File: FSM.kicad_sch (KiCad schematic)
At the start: 6 parts, among them U18 74HCT04, U23 74HCT02, U25 74HCT00, U27 74HCT02, U28 74HCT02, U9 74HCT74

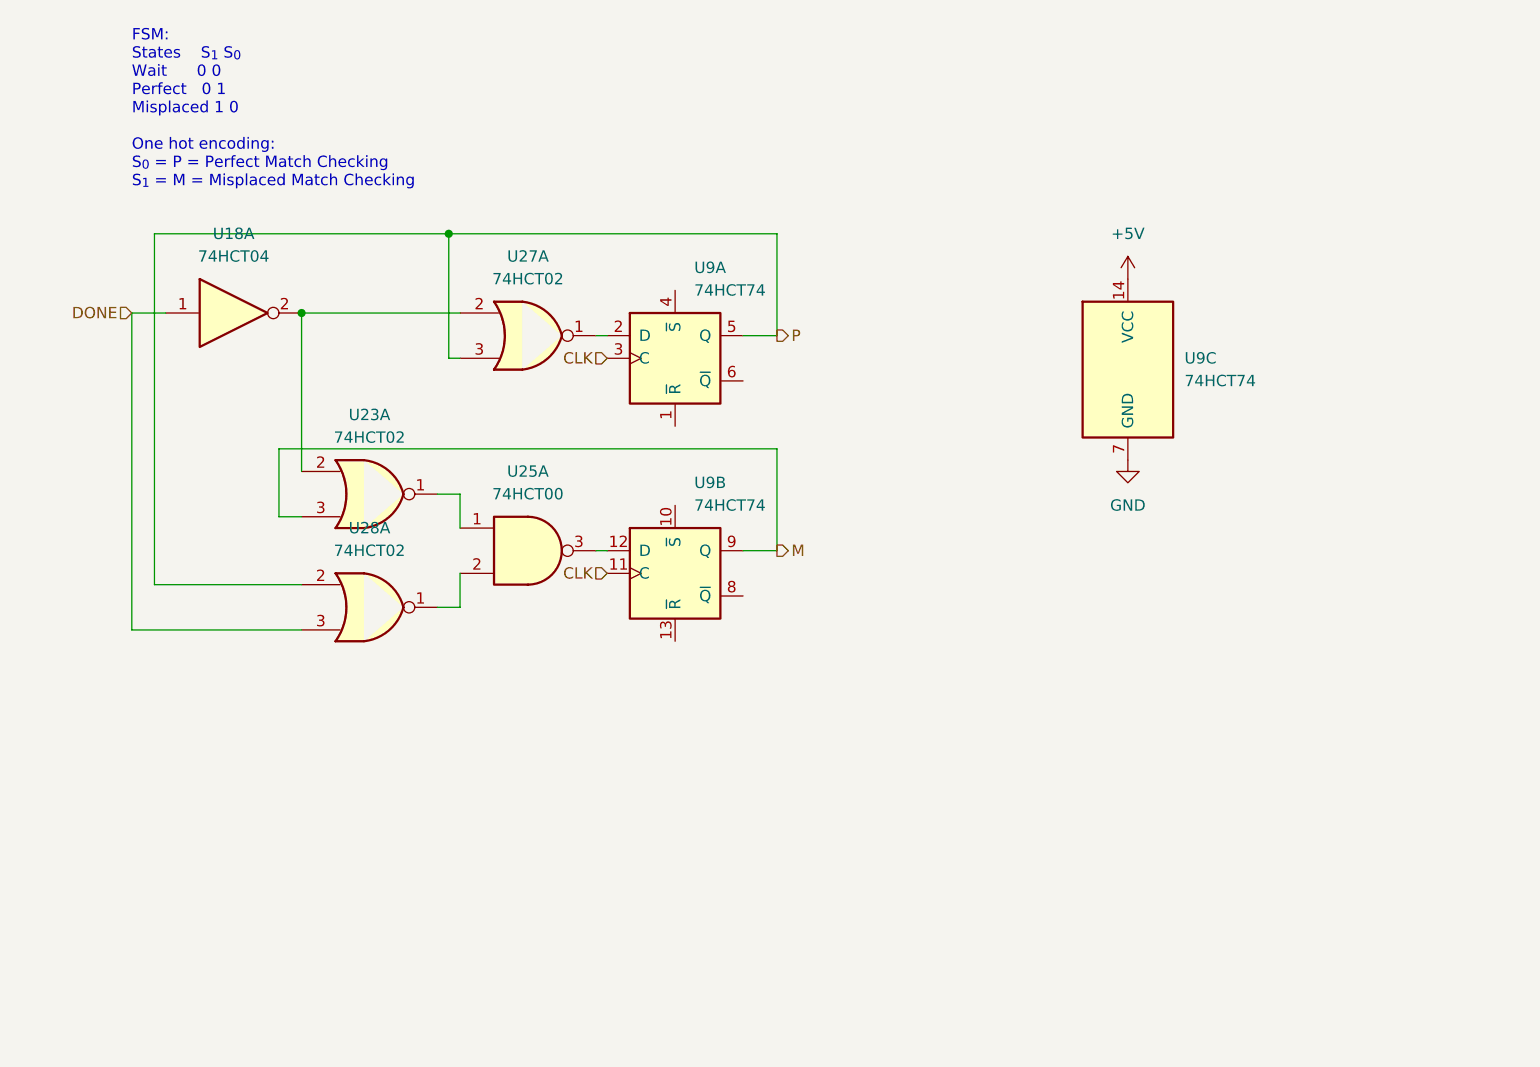
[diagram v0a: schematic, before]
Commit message: Added FSM, Button, 555 timer, changed shift registers
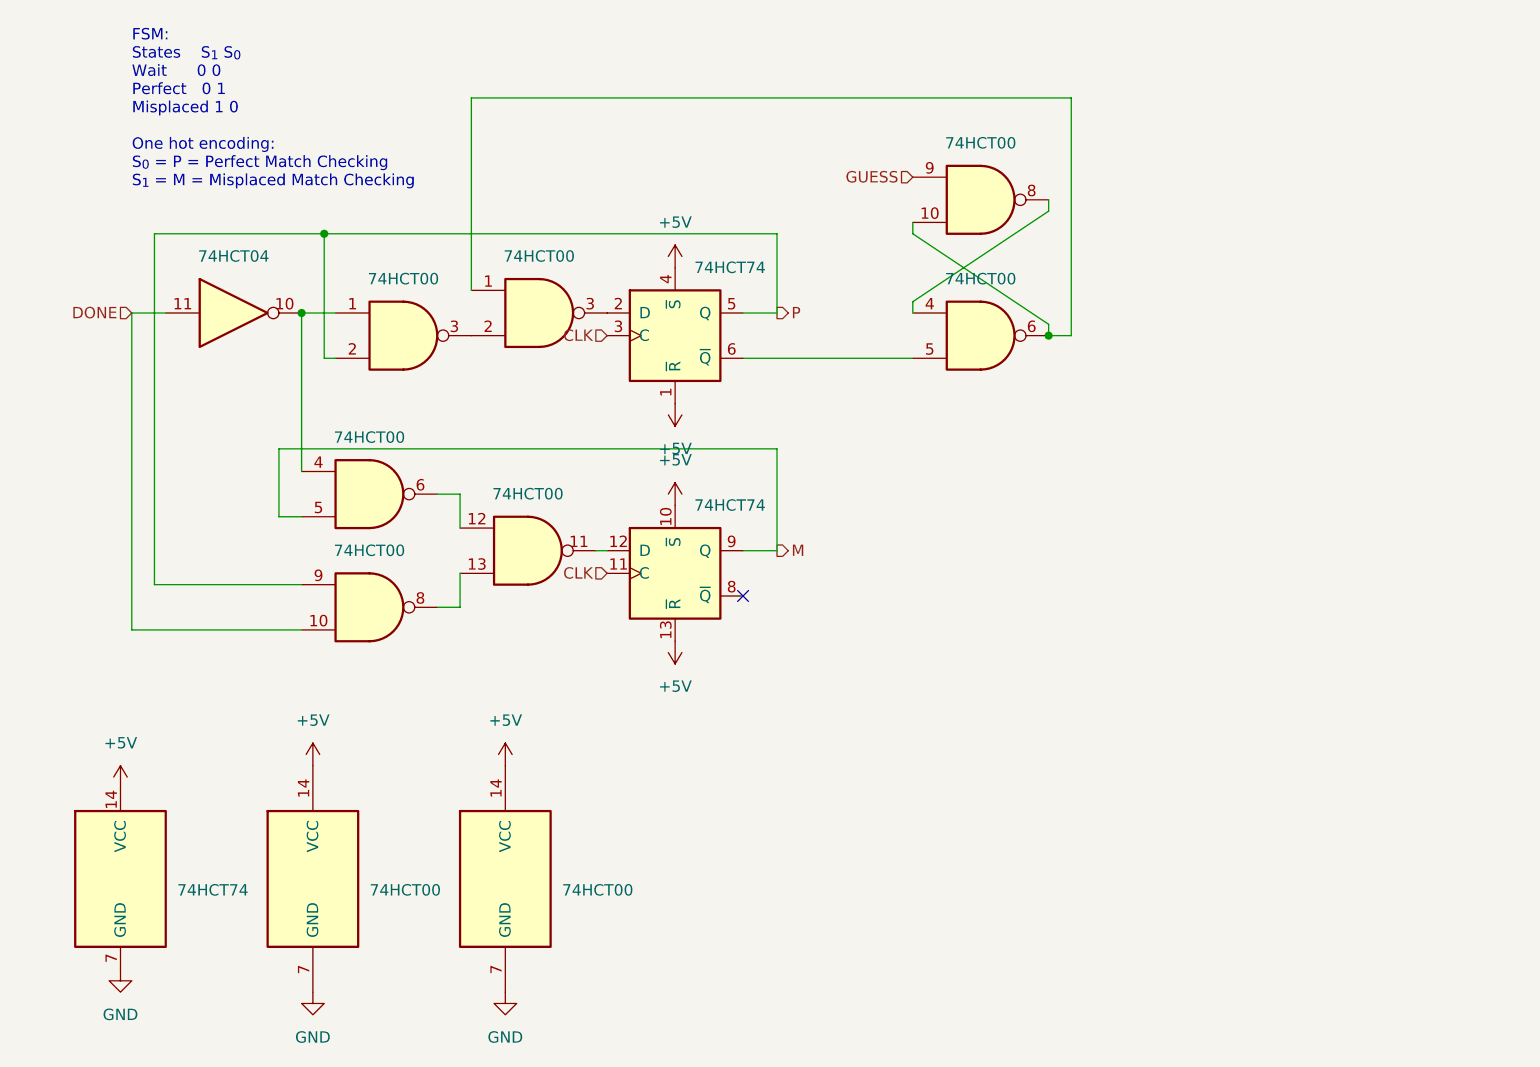
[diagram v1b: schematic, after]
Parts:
- added unit 2 of U22
- added U23: 74HCT00, symbol 74xx:74HCT00
- U22: renamed from U28; value 74HCT02 -> 74HCT00; symbol 74xx:74HCT02 -> 74xx:74HCT00
- U22: renamed from U27; value 74HCT02 -> 74HCT00; symbol 74xx:74HCT02 -> 74xx:74HCT00
- U22: renamed from U23; value 74HCT02 -> 74HCT00; symbol 74xx:74HCT02 -> 74xx:74HCT00
- renumbered U9 to U20, U25 to U22, U18 to U9
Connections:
- net +5V: now also U20.1 (~{R}), U20.10 (~{S}), U20.13 (~{R}), U20.4 (~{S}), U22.14 (VCC), U23.14 (VCC)
- net DONE: now also U22.10, U9.11; no longer U22.3, U9.1
- net GND: now also U22.7 (GND), U23.7 (GND)
- net M: now also U22.5; no longer U22.3
- net P: now also U22.2, U22.9; no longer U22.2, U22.3
- net at U20.2 (D): now also U23.3; no longer U22.1
- net at U20.6 (~{Q}): now also U23.5
- net at U20.12 (D): now also U22.11; no longer U22.3
- new net: U23.1, U23.10, U23.6
- new net: U23.4, U23.8
- new net: U22.13, U22.8
- new net: U22.3, U23.2
- new net: U22.1, U22.4, U9.10
- new net: U22.12, U22.6
- new net GUESS: U23.9
- no-connect marks 0 -> 1
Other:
- title: (none) -> FSM

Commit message: Fixes
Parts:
- added C3: 1u, symbol Device:C
- added C4: .01u, symbol Device:C
- added R3, R4: 10k, symbol Device:R
- added SW1: SW_Push, symbol Switch:SW_Push
- added U201: 40106, symbol 4xxx:40106
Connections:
- net +5V: now also C4.1, SW1.2
- net GND: now also R3.1, R4.1
- net Reset: now reaches U23.1, U23.10, U23.6
- net GUESS: no longer names the net of U23.9
- net GUESS: now also U201.2
- new net: C3.2, R4.2, U201.1
- new net: C3.1, C4.2, R3.2, SW1.1
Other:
- note added: "S_{0}^{+} = S_{0}DONE' + GUESS S_{1}^{+} = S_{1}DONE' + S_{0}DONE One hot encoding: S_{0} = P = Perfect Match Checking S_{1} = M = Misplaced Match Checking"
- note removed: "FSM: States S_{1} S_{0} Wait 0 0 Perfect 0 1 Misplaced 1 0 One hot encoding: S_{0} = P = Perfect Match Checking S_{1} = M = Misplaced Match Checking"

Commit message: Started PCB Work
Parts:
- C13: renamed from C4; footprint (none) -> Capacitor_SMD:C_0805_2012Metric_Pad1.18x1.45mm_HandSolder
- C14: renamed from C3; footprint (none) -> Capacitor_SMD:C_0805_2012Metric_Pad1.18x1.45mm_HandSolder
- R6: renamed from R4; footprint (none) -> Resistor_SMD:R_0805_2012Metric_Pad1.20x1.40mm_HandSolder
- R7: renamed from R3; footprint (none) -> Resistor_SMD:R_0805_2012Metric_Pad1.20x1.40mm_HandSolder
- SW2: renamed from SW1; footprint (none) -> Button_Switch_SMD:SW_SPST_Omron_B3FS-105xP
- U10: renamed from U201; footprint (none) -> Package_SO:SOIC-14_3.9x8.7mm_P1.27mm
- U22: renamed from U23; footprint (none) -> Package_SO:SOIC-14_3.9x8.7mm_P1.27mm
- U23: renamed from U20; footprint (none) -> Package_SO:SOIC-14_3.9x8.7mm_P1.27mm
- U24: renamed from U22; footprint (none) -> Package_SO:SOIC-14_3.9x8.7mm_P1.27mm
- U9: footprint (none) -> Package_SO:SOIC-14_3.9x8.7mm_P1.27mm
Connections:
- net +5V: now also U23.10 (~{S}), U23.4 (~{S}); no longer U23.1 (~{R}), U23.10 (~{S}), U23.13 (~{R}), U23.4 (~{S})
- net CLK: now also U23.11 (C), U23.3 (C); no longer U23.11 (C), U23.3 (C)
- net M: now also U23.5 (Q); no longer U23.9 (Q)
- net P: now also U23.9 (Q); no longer U23.5 (Q)
- net Reset: now also U22.11, U22.4; no longer U22.1, U22.6
- net at U22.8: now also U22.12; no longer U22.4
- net at U24.3: now also U22.5; no longer U22.2
- net at U24.11: now also U23.2 (D); no longer U23.12 (D)
- new net: U22.6, U23.12 (D)
- new net: U22.13, U23.8 (~{Q})
- new net PWR_ON_RST: U23.1 (~{R}), U23.13 (~{R})

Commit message: routed
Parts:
- C14: value 1u -> .1u
- renumbered R6 to R7, R7 to R8
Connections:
- net DONE: now also U24.2; no longer U24.10
- net M: now also U24.9; no longer U24.5
- net P: now also U24.1, U24.13; no longer U24.2, U24.9
- net Reset: now also U22.10, U22.2; no longer U22.10, U22.4
- net at C14.2, R7.2: now also U10.3; no longer U10.1
- net at U22.12: now also U22.3; no longer U22.8
- net at U23.12 (D): now also U22.8; no longer U22.6
- net at U23.2 (D): now also U24.6; no longer U24.11
- new net: U10.4, U22.1
- new net: U24.3, U24.4
- new net: U22.9, U24.11
- new net: U24.10, U24.12, U9.10
- new net: U24.5, U24.8
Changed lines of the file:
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@@
 		(on_board yes)
 		(dnp no)
-		(property "Reference" "R6"
+		(property "Reference" "R7"
 			(at 106.68 82.55 90)
 			(effects
@@
 			(project "ECE145Mastermind"
 				(path "/8c64fe8a-5d6b-41bc-b3a3-9bda7b2e0f2c/c249946c-91e3-42cd-8f8a-d6059405d3e8"
-					(reference "R6")
+					(reference "R7")
 					(unit 1)
 				)
@@
 		(at 110.49 53.34 0)
 		(mirror x)
-		(unit 3)
+		(unit 1)
 		(exclude_from_sim no)
 		(in_bom yes)
@@
 				(path "/8c64fe8a-5d6b-41bc-b3a3-9bda7b2e0f2c/c249946c-91e3-42cd-8f8a-d6059405d3e8"
 					(reference "U22")
-					(unit 3)
+					(unit 1)
 				)
 			)
@@
 		(lib_id "74xx:74HCT00")
 		(at 48.26 63.5 0)
-		(unit 3)
+		(unit 1)
 		(exclude_from_sim no)
 		(in_bom yes)
@@
 				(path "/8c64fe8a-5d6b-41bc-b3a3-9bda7b2e0f2c/c249946c-91e3-42cd-8f8a-d6059405d3e8"
 					(reference "U24")
-					(unit 3)
+					(unit 1)
 				)
 			)
@@
 		(dnp no)
 		(fields_autoplaced yes)
-		(property "Reference" "#PWR075"
+		(property "Reference" "#PWR076"
 			(at 20.32 95.25 0)
 			(effects
@@
 			(project ""
 				(path "/8c64fe8a-5d6b-41bc-b3a3-9bda7b2e0f2c/c249946c-91e3-42cd-8f8a-d6059405d3e8"
-					(reference "#PWR075")
+					(reference "#PWR076")
 					(unit 1)
 				)
@@
 		(lib_id "74xx:74HCT00")
 		(at 67.31 30.48 0)
-		(unit 2)
-		(exclude_from_sim no)
-		(in_bom yes)
-		(on_board yes)
-		(dnp no)
-		(fields_autoplaced yes)
+		(mirror x)
+		(unit 3)
+		(exclude_from_sim no)
+		(in_bom yes)
+		(on_board yes)
+		(dnp no)
 		(property "Reference" "U22"
-			(at 67.3017 21.59 0)
+			(at 67.3017 39.37 0)
 			(effects
 				(font
@@
 		)
 		(property "Value" "74HCT00"
-			(at 67.3017 24.13 0)
+			(at 67.3017 36.83 0)
 			(effects
 				(font
@@
 				(path "/8c64fe8a-5d6b-41bc-b3a3-9bda7b2e0f2c/c249946c-91e3-42cd-8f8a-d6059405d3e8"
 					(reference "U22")
-					(unit 2)
+					(unit 3)
 				)
 			)
@@
 		(dnp no)
 		(fields_autoplaced yes)
-		(property "Reference" "#PWR080"
+		(property "Reference" "#PWR081"
 			(at 63.5 132.08 0)
 			(effects
@@
 			(project "ECE145Mastermind"
 				(path "/8c64fe8a-5d6b-41bc-b3a3-9bda7b2e0f2c/c249946c-91e3-42cd-8f8a-d6059405d3e8"
-					(reference "#PWR080")
+					(reference "#PWR081")
 					(unit 1)
 				)
@@
 		(fields_autoplaced yes)
 		(property "Reference" "C14"
-			(at 99.06 81.2801 0)
-			(effects
-				(font
-					(size 1.27 1.27)
-				)
-				(justify left)
-			)
-		)
-		(property "Value" "1u"
-			(at 99.06 78.7401 0)
-			(effects
-				(font
-					(size 1.27 1.27)
-				)
-				(justify left)
+			(at 106.68 78.7399 0)
+			(effects
+				(font
+					(size 1.27 1.27)
+				)
+				(justify right)
+			)
+		)
+		(property "Value" ".1u"
+			(at 106.68 81.2799 0)
+			(effects
+				(font
+					(size 1.27 1.27)
+				)
+				(justify right)
 			)
 		)
@@
 		(dnp no)
 		(fields_autoplaced yes)
-		(property "Reference" "#PWR084"
+		(property "Reference" "#PWR085"
 			(at 116.84 76.2 0)
 			(effects
@@
 			(project "ECE145Mastermind"
 				(path "/8c64fe8a-5d6b-41bc-b3a3-9bda7b2e0f2c/c249946c-91e3-42cd-8f8a-d6059405d3e8"
-					(reference "#PWR084")
+					(reference "#PWR085")
 					(unit 1)
 				)
@@
 		(dnp no)
 		(fields_autoplaced yes)
-		(property "Reference" "#PWR082"
+		(property "Reference" "#PWR083"
 			(at 82.55 55.88 0)
 			(effects
@@
 			(project ""
 				(path "/8c64fe8a-5d6b-41bc-b3a3-9bda7b2e0f2c/c249946c-91e3-42cd-8f8a-d6059405d3e8"
-					(reference "#PWR082")
+					(reference "#PWR083")
 					(unit 1)
 				)
@@
 		(dnp no)
 		(fields_autoplaced yes)
-		(property "Reference" "#PWR078"
+		(property "Reference" "#PWR079"
 			(at 41.91 132.08 0)
 			(effects
@@
 			(project ""
 				(path "/8c64fe8a-5d6b-41bc-b3a3-9bda7b2e0f2c/c249946c-91e3-42cd-8f8a-d6059405d3e8"
-					(reference "#PWR078")
+					(reference "#PWR079")
 					(unit 1)
 				)
@@
 		(dnp no)
 		(fields_autoplaced yes)
-		(property "Reference" "#PWR076"
+		(property "Reference" "#PWR077"
 			(at 20.32 129.54 0)
 			(effects
@@
 			(project ""
 				(path "/8c64fe8a-5d6b-41bc-b3a3-9bda7b2e0f2c/c249946c-91e3-42cd-8f8a-d6059405d3e8"
-					(reference "#PWR076")
+					(reference "#PWR077")
 					(unit 1)
 				)
@@
 		(fields_autoplaced yes)
 		(property "Reference" "U22"
-			(at 110.4817 46.99 0)
+			(at 110.4817 29.21 0)
 			(effects
 				(font
@@
 		(dnp no)
 		(fields_autoplaced yes)
-		(property "Reference" "#PWR083"
+		(property "Reference" "#PWR084"
 			(at 102.87 101.6 0)
 			(effects
@@
 			(project "ECE145Mastermind"
 				(path "/8c64fe8a-5d6b-41bc-b3a3-9bda7b2e0f2c/c249946c-91e3-42cd-8f8a-d6059405d3e8"
-					(reference "#PWR083")
+					(reference "#PWR084")
 					(unit 1)
 				)
@@
 		(dnp no)
 		(fields_autoplaced yes)
-		(property "Reference" "#PWR079"
+		(property "Reference" "#PWR080"
 			(at 63.5 104.14 0)
 			(effects
@@
 			(project "ECE145Mastermind"
 				(path "/8c64fe8a-5d6b-41bc-b3a3-9bda7b2e0f2c/c249946c-91e3-42cd-8f8a-d6059405d3e8"
-					(reference "#PWR079")
+					(reference "#PWR080")
 					(unit 1)
 				)
@@
 		(dnp no)
 		(fields_autoplaced yes)
-		(property "Reference" "#PWR077"
+		(property "Reference" "#PWR078"
 			(at 41.91 104.14 0)
 			(effects
@@
 			(project ""
 				(path "/8c64fe8a-5d6b-41bc-b3a3-9bda7b2e0f2c/c249946c-91e3-42cd-8f8a-d6059405d3e8"
-					(reference "#PWR077")
+					(reference "#PWR078")
 					(unit 1)
 				)
@@
 		(on_board yes)
 		(dnp no)
-		(property "Reference" "R7"
+		(property "Reference" "R8"
 			(at 106.68 90.17 90)
 			(effects
@@
 			(project "ECE145Mastermind"
 				(path "/8c64fe8a-5d6b-41bc-b3a3-9bda7b2e0f2c/c249946c-91e3-42cd-8f8a-d6059405d3e8"
-					(reference "R7")
+					(reference "R8")
 					(unit 1)
 				)
@@
 		(lib_id "4xxx:40106")
 		(at 102.87 68.58 90)
-		(unit 1)
+		(unit 2)
 		(exclude_from_sim no)
 		(in_bom yes)
@@
 				(path "/8c64fe8a-5d6b-41bc-b3a3-9bda7b2e0f2c/c249946c-91e3-42cd-8f8a-d6059405d3e8"
 					(reference "U10")
-					(unit 1)
+					(unit 2)
 				)
 			)
@@
 		(lib_id "74xx:74HCT00")
 		(at 66.04 57.15 0)
-		(unit 4)
-		(exclude_from_sim no)
-		(in_bom yes)
-		(on_board yes)
-		(dnp no)
-		(fields_autoplaced yes)
+		(mirror x)
+		(unit 2)
+		(exclude_from_sim no)
+		(in_bom yes)
+		(on_board yes)
+		(dnp no)
 		(property "Reference" "U24"
-			(at 66.0317 48.26 0)
+			(at 66.0317 66.04 0)
 			(effects
 				(font
@@
 		)
 		(property "Value" "74HCT00"
-			(at 66.0317 50.8 0)
+			(at 66.0317 63.5 0)
 			(effects
 				(font
@@
 				(path "/8c64fe8a-5d6b-41bc-b3a3-9bda7b2e0f2c/c249946c-91e3-42cd-8f8a-d6059405d3e8"
 					(reference "U24")
-					(unit 4)
+					(unit 2)
 				)
 			)
@@
 		(dnp no)
 		(fields_autoplaced yes)
-		(property "Reference" "#PWR085"
+		(property "Reference" "#PWR086"
 			(at 116.84 83.82 0)
 			(effects
@@
 			(project "ECE145Mastermind"
 				(path "/8c64fe8a-5d6b-41bc-b3a3-9bda7b2e0f2c/c249946c-91e3-42cd-8f8a-d6059405d3e8"
-					(reference "#PWR085")
+					(reference "#PWR086")
 					(unit 1)
 				)
@@
 		(lib_id "74xx:74HCT00")
 		(at 52.07 33.02 0)
-		(unit 1)
+		(unit 4)
 		(exclude_from_sim no)
 		(in_bom yes)
@@
 				(path "/8c64fe8a-5d6b-41bc-b3a3-9bda7b2e0f2c/c249946c-91e3-42cd-8f8a-d6059405d3e8"
 					(reference "U24")
-					(unit 1)
+					(unit 4)
 				)
 			)
@@
 		(lib_id "74xx:74HCT00")
 		(at 48.26 50.8 0)
-		(unit 2)
-		(exclude_from_sim no)
-		(in_bom yes)
-		(on_board yes)
-		(dnp no)
-		(fields_autoplaced yes)
+		(mirror x)
+		(unit 3)
+		(exclude_from_sim no)
+		(in_bom yes)
+		(on_board yes)
+		(dnp no)
 		(property "Reference" "U24"
-			(at 48.2517 41.91 0)
+			(at 48.2517 59.69 0)
 			(effects
 				(font
@@
 		)
 		(property "Value" "74HCT00"
-			(at 48.2517 44.45 0)
+			(at 48.2517 57.15 0)
 			(effects
 				(font
@@
 				(path "/8c64fe8a-5d6b-41bc-b3a3-9bda7b2e0f2c/c249946c-91e3-42cd-8f8a-d6059405d3e8"
 					(reference "U24")
-					(unit 2)
+					(unit 3)
 				)
 			)
@@
 		(dnp no)
 		(fields_autoplaced yes)
-		(property "Reference" "#PWR081"
+		(property "Reference" "#PWR082"
 			(at 82.55 29.21 0)
 			(effects
@@
 			(project ""
 				(path "/8c64fe8a-5d6b-41bc-b3a3-9bda7b2e0f2c/c249946c-91e3-42cd-8f8a-d6059405d3e8"
-					(reference "#PWR081")
+					(reference "#PWR082")
 					(unit 1)
 				)

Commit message: Ground and Power Plane?
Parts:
- SW2: footprint Button_Switch_SMD:SW_SPST_Omron_B3FS-105xP -> Button_Switch_THT:SW_SPST_Omron_B3F-40xx
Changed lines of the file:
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@@
 			)
 		)
-		(property "Footprint" "Button_Switch_SMD:SW_SPST_Omron_B3FS-105xP"
+		(property "Footprint" "Button_Switch_THT:SW_SPST_Omron_B3F-40xx"
 			(at 107.95 88.9 0)
 			(effects

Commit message: Finished?
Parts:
- added TP6: P, TestPoint:TestPoint_Pad_1.5x1.5mm, symbol Connector:TestPoint_Small
- added TP7: M, TestPoint:TestPoint_Pad_1.5x1.5mm, symbol Connector:TestPoint_Small
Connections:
- net M: now also TP7.1
- net P: now also TP6.1

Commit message: Final touches
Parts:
- renumbered TP7 to TP8, TP6 to TP9, U10 to U14
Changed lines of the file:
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@@
 		(dnp no)
 		(fields_autoplaced yes)
-		(property "Reference" "TP6"
+		(property "Reference" "TP9"
 			(at 100.33 29.2099 0)
 			(show_name no)
@@
 			(project "ECE145Mastermind"
 				(path "/8c64fe8a-5d6b-41bc-b3a3-9bda7b2e0f2c/c249946c-91e3-42cd-8f8a-d6059405d3e8"
-					(reference "TP6")
+					(reference "TP9")
 					(unit 1)
 				)
@@
 		(in_pos_files yes)
 		(dnp no)
-		(property "Reference" "U10"
+		(property "Reference" "U14"
 			(at 97.79 69.8501 90)
 			(show_name no)
@@
 			(project "ECE145Mastermind"
 				(path "/8c64fe8a-5d6b-41bc-b3a3-9bda7b2e0f2c/c249946c-91e3-42cd-8f8a-d6059405d3e8"
-					(reference "U10")
+					(reference "U14")
 					(unit 2)
 				)
@@
 		(dnp no)
 		(fields_autoplaced yes)
-		(property "Reference" "TP7"
+		(property "Reference" "TP8"
 			(at 99.06 55.8799 0)
 			(show_name no)
@@
 			(project "ECE145Mastermind"
 				(path "/8c64fe8a-5d6b-41bc-b3a3-9bda7b2e0f2c/c249946c-91e3-42cd-8f8a-d6059405d3e8"
-					(reference "TP7")
+					(reference "TP8")
 					(unit 1)
 				)
